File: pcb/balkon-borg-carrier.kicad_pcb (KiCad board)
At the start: 2 copper layers, 150 x 92 mm, 37 parts, among them J2 ESP32-DevKitC L, J3 ESP32-DevKitC R, Q1 BC337, Q2 BC337, Q3 BC337, Q4 BC337

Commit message: pcb: run final routing pass and add GND pour
The netlist fixes (radial F1, 4-pin radar connector, M2.5 holes) had never
been imported into the committed board, so it was stale. Rebuild the board
from the netlist end to end: kinet2pcb makes a fresh .kicad_pcb, place-board
lays it out and sets the Aisler DRC minimums, Freerouting autoroutes it and
apply-ses imports the session back. Result: 231 tracks, 3 vias, 0 unconnected.

add-ground-pour.py then fills a GND pour on both layers with thermal reliefs
on the THT pads and a no-copper rule area under the DevKit antenna. The
socketed ESP header GND pins bond straight to the plane through their routed
tracks (zone-connection NONE), which also clears a starved-thermal island the
dense header fan-out would otherwise pinch off. DRC against the Aisler
minimums is clean: 0 violations.

The pour runs in three separate pcbnew processes (make pour): a rule area is
dropped on save if a pad zone-connection was set, or a fill ran, in the same
session.

Co-Authored-By: Claude Fable 5 <noreply@anthropic.com>
Claude-Session: https://claude.ai/code/session_01X3XcqyQcw3eP146g1EdqWY
Signed-off-by: Hagen Paul Pfeifer <hagen@jauu.net>
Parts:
- removed the J_RADAR at (105.0, 9.00)
- removed R16: 1k, Resistor_THT:R_Axial_DIN0207_L6.3mm_D2.5mm_P10.16mm_Horizontal
- added J_RADAR: LD2410B, Connector_JST:JST_XH_B4B-XH-A_1x04_P2.50mm_Vertical, F.Cu at (105.0, 9.00)
- F1: footprint Resistor_THT:R_Axial_DIN0207_L6.3mm_D2.5mm_P10.16mm_Horizontal -> Capacitor_THT:C_Disc_D7.5mm_W5.0mm_P5.00mm
- H1, H2, H3, H4: value MountingHole_3.2mm_M3 -> MountingHole_2.7mm_M2.5; footprint MountingHole_3.2mm_M3 -> MountingHole_2.7mm_M2.5
- R10, R12, R14: value 1k -> 100
- R11, R13, R15, R9: value 100 -> 1k
- R3: value 220 -> 4k7
- R5: value 4k7 -> 100
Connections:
- J2 pad 10: N$16 -> N$15
- J2 pad 11: N$13 -> N$12
- J2 pad 12: N$10 -> N$9
- J2 pad 15: N$7 -> N$6
- J2 pad 5: N$3 -> (no net)
- J2 pad 7: N$4 -> N$3
- J2 pad 8: N$5 -> N$4
- J2 pad 9: N$6 -> N$5
- J3 pad 13: N$9 -> N$8
- J3 pad 2: N$12 -> N$11
- J3 pad 8: N$18 -> N$17
- J3 pad 9: N$15 -> N$14
- Q1 pad 2: N$8 -> N$7
- Q2 pad 2: N$11 -> N$10
- Q3 pad 2: N$14 -> N$13
- Q4 pad 2: N$17 -> N$16
- R10 pad 1: N$8 -> BTN2_SW
- R11 pad 1: BTN2_SW -> N$10
- R11 pad 2: N$10 -> N$11
- R12 pad 1: N$11 -> BTN3_SW
- R13 pad 1: BTN3_SW -> N$13
- R13 pad 2: N$13 -> N$14
- R14 pad 1: N$14 -> BTN4_SW
- R15 pad 1: BTN4_SW -> N$16
- R15 pad 2: N$16 -> N$17
- R3 pad 1: RADAR_OUT -> I2C_SDA
- R3 pad 2: N$3 -> +3V3
- R4 pad 1: I2C_SDA -> I2C_SCL
- R5 pad 1: I2C_SCL -> ENC_A
- R5 pad 2: +3V3 -> N$3
- R6 pad 1: ENC_A -> ENC_B
- R7 pad 1: ENC_B -> ENC_SW
- R8 pad 1: ENC_SW -> BTN1_SW
- R9 pad 1: BTN1_SW -> N$7
- R9 pad 2: N$7 -> N$8
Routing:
- net RADAR_OUT: track 85.2 -> 0.00 mm
- net BTN1_SW: track 89.0 -> 23.1 mm
- net N$18: track 47.1 -> 0.00 mm, vias 1 -> 0
- net N$15: track 30.8 -> 66.5 mm
- net N$8: track 76.9 -> 45.2 mm, vias 2 -> 0
- net N$16: track 61.0 -> 30.5 mm
- net GND: track 373.8 -> 345.2 mm
- net N$13: track 56.8 -> 28.6 mm
- net N$9: track 36.9 -> 61.2 mm
- net N$17: track 28.0 -> 47.5 mm
- net N$6: track 24.9 -> 10.5 mm
- net N$11: track 44.7 -> 30.9 mm, vias 0 -> 1
- net N$12: track 41.4 -> 55.2 mm
- net +3V3: track 130.6 -> 117.4 mm
- net N$10: track 59.9 -> 50.7 mm, vias 1 -> 0
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- added copper zone on B.Cu, net GND
- added copper zone on F.Cu, net GND

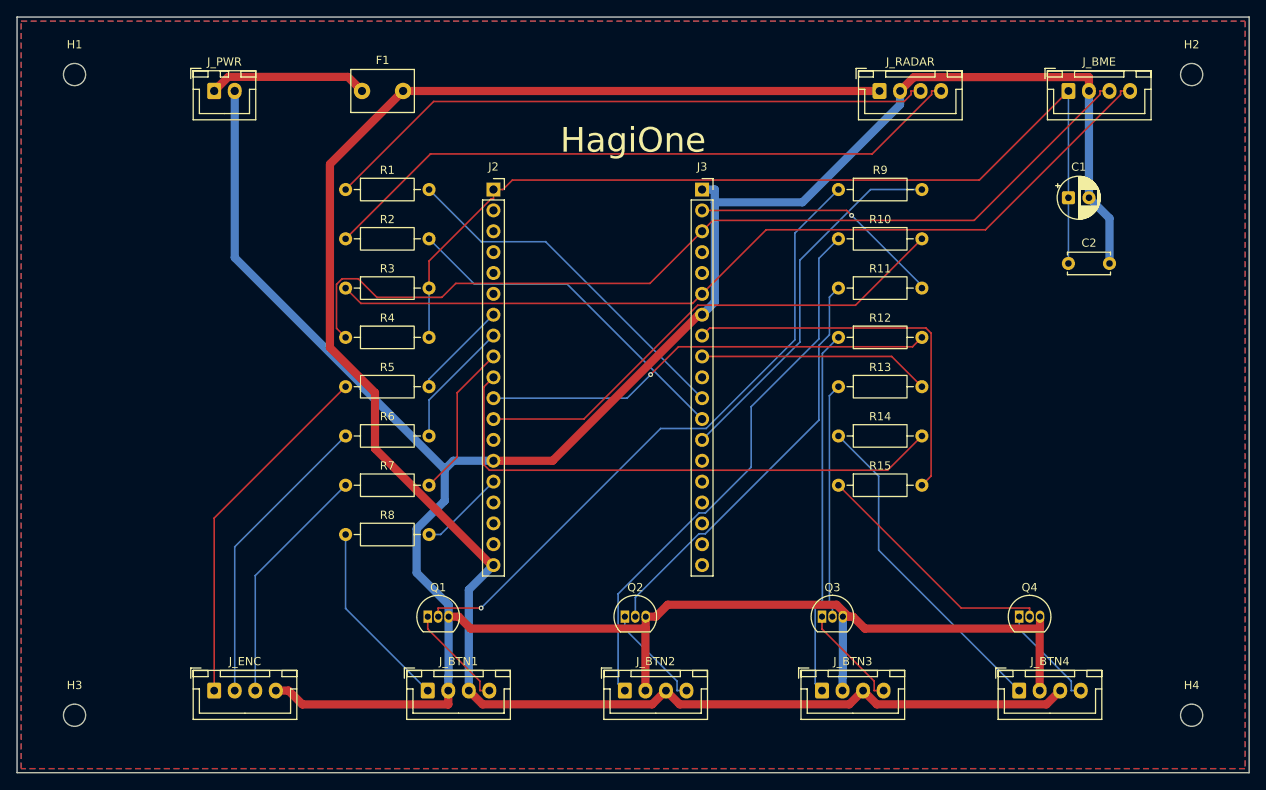
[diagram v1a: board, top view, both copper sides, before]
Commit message: pcb: re-place connectors to match cable exits and re-route
Freeze the JST connector positions to the enclosure cable targets
(docs/wiring.md) and re-route the whole board:

  - button/encoder connectors on the right short edge (toward the +X end
    wall), each button's NPN driver just inboard;
  - power, radar and BME on the down edge (toward the floor tower/BME and
    the gland);
  - ESP headers left of centre, decoupling by the 3V3 pin, the 15 series
    resistors in three tidy rows below the ESP;
  - "HagiOne" silk moved to the clear strip left of the ESP.

Re-routed with Freerouting: 293 tracks, 5 vias, 0 unconnected. Pour
redone (antenna keep-out moved to the new ESP position; all GND pads
except J_PWR set to no zone connection to kill starved-thermal islands in
the denser layout and ease hand-soldering). DRC clean: 0 violations
including silkscreen.

ESP row spacing stays 25.4 mm: buy the official Espressif DevKitC-V4
(reichelt #341303 / DigiKey ESP32-DEVKITC-32E), not a 0.9-inch clone.

Co-Authored-By: Claude Fable 5 <noreply@anthropic.com>
Claude-Session: https://claude.ai/code/session_01X3XcqyQcw3eP146g1EdqWY
Signed-off-by: Hagen Paul Pfeifer <hagen@jauu.net>
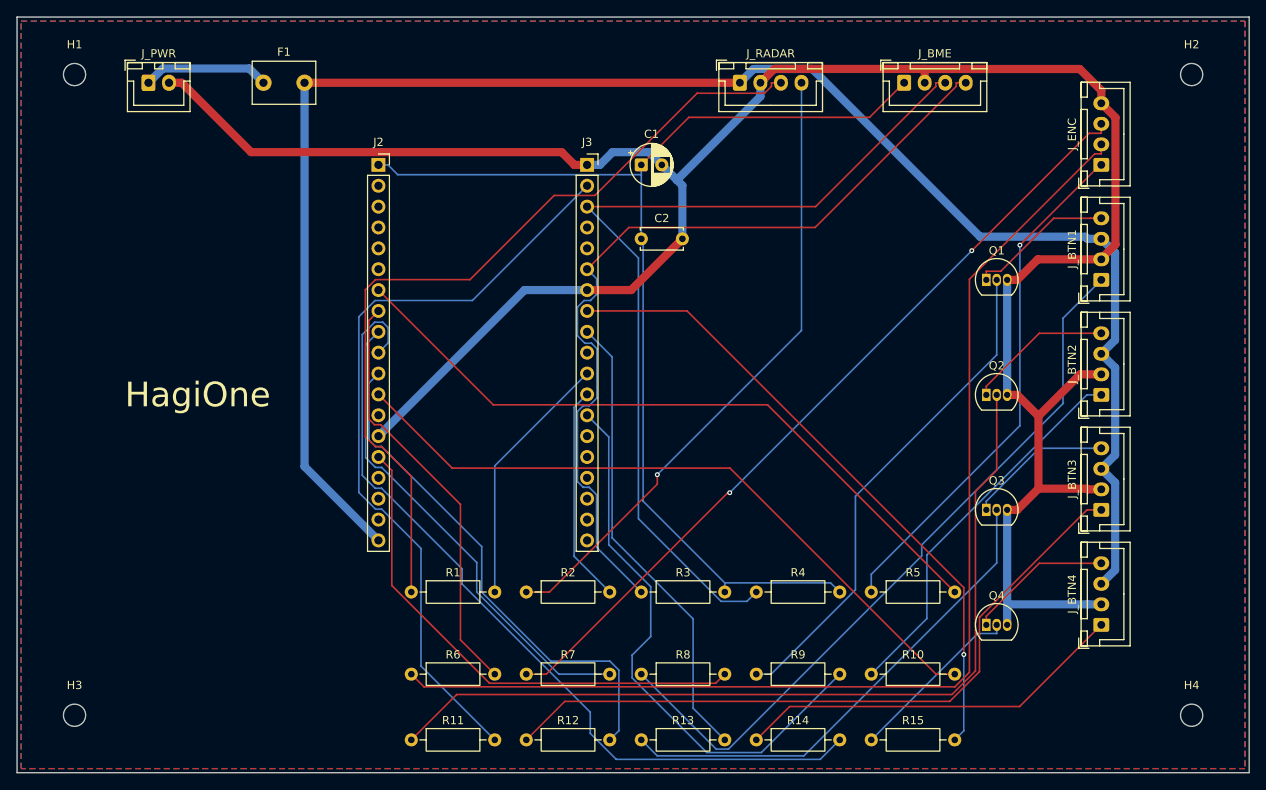
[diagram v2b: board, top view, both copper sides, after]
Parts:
- moved J_ENC 125.5 mm to (132.0, 18.0), turned to 90 degrees
- moved J_BTN1 96.0 mm to (132.0, 32.0), turned to 90 degrees
- moved Q1 79.4 mm to (118.0, 32.0)
- moved R11 75.7 mm to (48.0, 88.0)
- moved R5 68.7 mm to (104.0, 70.0)
- moved J_BTN2 68.3 mm to (132.0, 46.0), turned to 90 degrees
- moved R12 62.0 mm to (62.0, 88.0)
- moved R9 59.8 mm to (90.0, 80.0)
- moved R4 58.8 mm to (90.0, 70.0)
- moved R10 53.2 mm to (104.0, 80.0)
- moved C1 52.2 mm to (76.0, 18.0)
- moved C2 52.1 mm to (76.0, 27.0)
- moved R3 51.6 mm to (76.0, 70.0)
- moved Q2 51.6 mm to (118.0, 46.0)
- moved R1 49.6 mm to (48.0, 70.0)
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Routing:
- net ENC_B: track 36.6 -> 140.7 mm
- net N$3: track 12.0 -> 85.4 mm
- net ENC_SW: track 29.6 -> 98.4 mm, vias 0 -> 2
- net BTN1_SW: track 23.1 -> 90.3 mm
- net N$11: track 30.9 -> 93.2 mm, vias 1 -> 0
- net N$10: track 50.7 -> 106.8 mm
- net N$6: track 10.5 -> 62.2 mm
- net GND: track 345.2 -> 293.5 mm
- net BTN3_SW: track 44.5 -> 85.5 mm
- net N$5: track 18.9 -> 58.7 mm
- net N$4: track 15.5 -> 51.5 mm
- net N$15: track 66.5 -> 100.8 mm
- net N$13: track 28.6 -> 60.3 mm
- net N$17: track 47.5 -> 78.8 mm, vias 0 -> 1
- net N$14: track 28.3 -> 56.6 mm
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
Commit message: pcb: brand silkscreen "Balkon Borg" with "by HagiOne"
Replace the single "HagiOne" silk with "Balkon Borg" and a smaller
"by HagiOne" underneath, in the clear strip left of the ESP. DRC clean
(0 violations incl. silkscreen); outputs and board image refreshed.

Co-Authored-By: Claude Fable 5 <noreply@anthropic.com>
Claude-Session: https://claude.ai/code/session_01X3XcqyQcw3eP146g1EdqWY
Signed-off-by: Hagen Paul Pfeifer <hagen@jauu.net>
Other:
- board text added: "Balkon Borg"
- board text added: "by HagiOne"
- board text removed: "HagiOne"
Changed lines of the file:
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@@
 		(layer "Edge.Cuts")
 	)
-	(gr_text "HagiOne"
-		(at 22 46 0)
+	(gr_text "by HagiOne"
+		(at 22 50 0)
 		(layer "F.SilkS")
 		(effects
 			(font
-				(size 3 3)
-				(thickness 0.5)
+				(size 1.5 1.5)
+				(thickness 0.25)
 			)
 		)
+	)
+	(gr_text "Balkon Borg"
+		(at 22 44 0)
+		(layer "F.SilkS")
+		(effects
+			(font
+				(size 2.5 2.5)
+				(thickness 0.4)
+			)
+		)
